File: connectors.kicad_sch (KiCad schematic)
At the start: 4 parts, among them J1 Conn_01x04_Pin, J2 Conn_01x04_Pin, J3 Conn_01x09_Pin, J4 Conn_02x03_Odd_Even

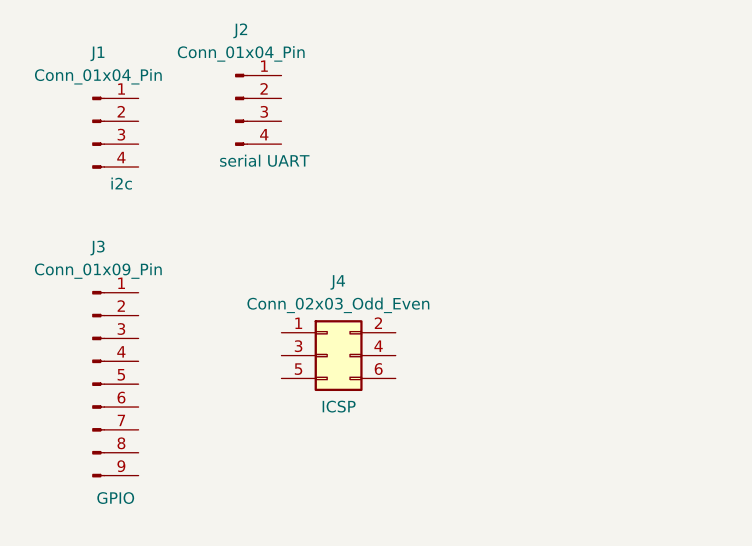
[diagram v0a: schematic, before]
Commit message: assigned footprints
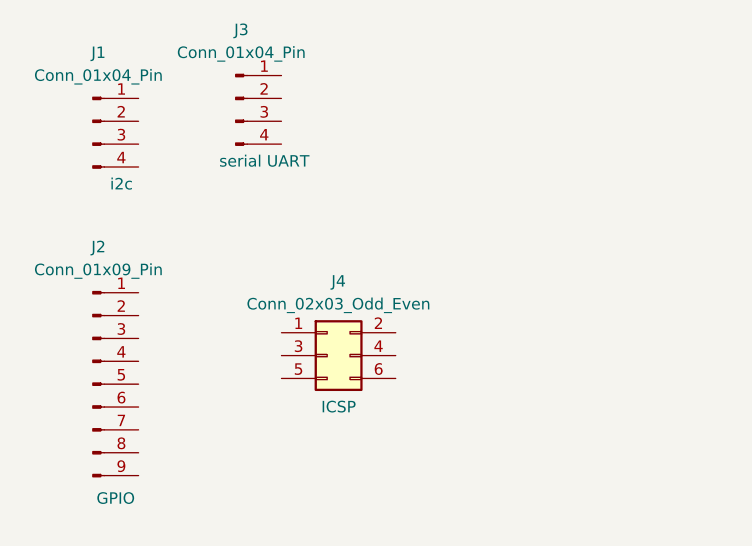
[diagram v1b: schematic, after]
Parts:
- J1: footprint (none) -> Connector_PinHeader_2.54mm:PinHeader_1x04_P2.54mm_Vertical
- J2: renamed from J3; footprint (none) -> Connector_PinHeader_2.54mm:PinHeader_1x09_P2.54mm_Vertical
- J3: renamed from J2; footprint (none) -> Connector_PinHeader_2.54mm:PinHeader_1x04_P2.54mm_Vertical
- J4: footprint (none) -> Connector_PinHeader_2.54mm:PinHeader_2x03_P2.54mm_Vertical
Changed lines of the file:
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@@
 		(in_pos_files yes)
 		(dnp no)
-		(property "Reference" "J3"
+		(property "Reference" "J2"
 			(at 103.505 92.71 0)
 			(show_name no)
@@
 			)
 		)
-		(property "Footprint" ""
+		(property "Footprint" "Connector_PinHeader_2.54mm:PinHeader_1x09_P2.54mm_Vertical"
 			(at 102.87 107.95 0)
 			(hide yes)
@@
 			(project "MCU Datalogger"
 				(path "/b73ecac8-4a36-487b-b5fb-782ebc8b8ea9/2c854e0b-a623-46a9-a005-dfed31ab0568"
-					(reference "J3")
+					(reference "J2")
 					(unit 1)
 				)
@@
 			)
 		)
-		(property "Footprint" ""
+		(property "Footprint" "Connector_PinHeader_2.54mm:PinHeader_2x03_P2.54mm_Vertical"
 			(at 128.905 104.775 0)
 			(hide yes)
@@
 			)
 		)
-		(property "Footprint" ""
+		(property "Footprint" "Connector_PinHeader_2.54mm:PinHeader_1x04_P2.54mm_Vertical"
 			(at 102.87 78.74 0)
 			(hide yes)
@@
 		(in_pos_files yes)
 		(dnp no)
-		(property "Reference" "J2"
+		(property "Reference" "J3"
 			(at 119.38 68.58 0)
 			(show_name no)
@@
 			)
 		)
-		(property "Footprint" ""
+		(property "Footprint" "Connector_PinHeader_2.54mm:PinHeader_1x04_P2.54mm_Vertical"
 			(at 118.745 76.2 0)
 			(hide yes)
@@
 			(project "MCU Datalogger"
 				(path "/b73ecac8-4a36-487b-b5fb-782ebc8b8ea9/2c854e0b-a623-46a9-a005-dfed31ab0568"
-					(reference "J2")
+					(reference "J3")
 					(unit 1)
 				)

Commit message: wiring on sheet 2 done
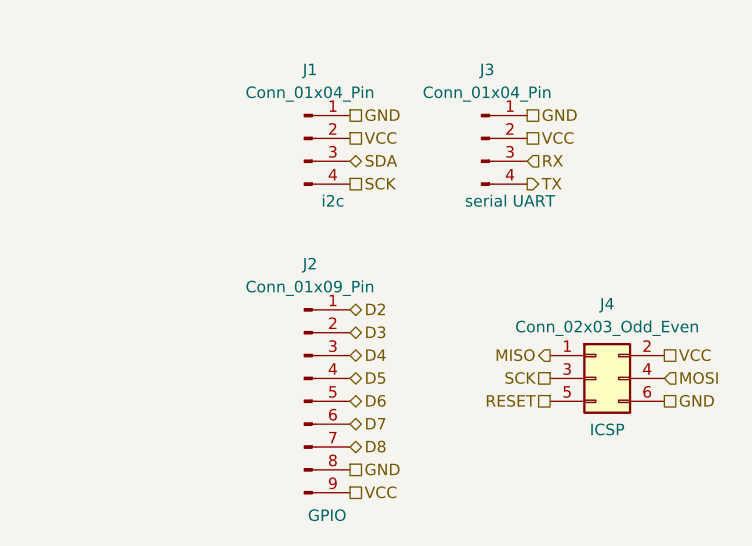
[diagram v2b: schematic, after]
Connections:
- net D2: now reaches J2.1 (Pin_1)
- net D3: now reaches J2.2 (Pin_2)
- net D4: now reaches J2.3 (Pin_3)
- net D5: now reaches J2.4 (Pin_4)
- net D6: now reaches J2.5 (Pin_5)
- net D7: now reaches J2.6 (Pin_6)
- net D8: now reaches J2.7 (Pin_7)
- net GND: now reaches J2.8 (Pin_8)
- net GND: now also J1.1 (Pin_1), J3.1 (Pin_1), J4.6 (Pin_6)
- net VCC: now reaches J2.9 (Pin_9)
- net VCC: now also J1.2 (Pin_2), J3.2 (Pin_2), J4.2 (Pin_2)
- net MISO: now reaches J4.1 (Pin_1)
- net SCK: now reaches J4.3 (Pin_3)
- net SCK: now also J1.4 (Pin_4)
- net MOSI: now reaches J4.4 (Pin_4)
- net RESET: now reaches J4.5 (Pin_5)
- net SDA: now reaches J1.3 (Pin_3)
- net RX: now reaches J3.3 (Pin_3)
- net TX: now reaches J3.4 (Pin_4)
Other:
- moved on the sheet: J1, J2, J3, J4
